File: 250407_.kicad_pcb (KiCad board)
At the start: 2 copper layers, 390 x 180.2 mm, 227 parts, among them CN1 KEYBOARD_20PIN_MALE, CN10 LED_CONNECTOR, CN2 USER_PORT_CON, CN3 CASSETTE_PORT_CON, CN4 SERIAL_BUS_CON, CN5 AV_CONN, CN6 EXPANSION_PORT, CN7 POWER_CON, CN8 CONTROL_PORT, CN9 CONTROL_PORT, M1 MODULATOR_LONGBOARD, Q1 2SC1815, Q2 2SC1815, Q3 TP298/2SD880, Q7 2SC1815, Q8 2SC1815, SW1 POWER_SWITCH, U1 CIA_U1, U10 4164-2, U11 4164-2, U12 4164-2, U13 74LS257, U14 74LS258, U15 74LS139, U16 4066_U28, U17 PLA_U17, U18 6581, U19 VIC, U2 CIA_U2, U20 556, U21 4164-2, U22 4164-2, U23 4164-2, U24 4164-2, U25 74LS257, U26 74LS373, U27 7408_U27, U28 4066_U28, U29 74LS74, U3 2364A, U30 74LS193, U31 74LS629N, U32 MC4044, U4 2364A, U5 2332A, U6 2114, U7 6510_MPU, U8 7406N, U9 4164-2, Y1 Crystal

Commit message: TP29B #2
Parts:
- Q3: value TP298/2SD880 -> TP29B/2SD880
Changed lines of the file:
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@@
       (effects (font (size 1.5 1.5) (thickness 0.25)))
     )
-    (fp_text value TP298/2SD880 (at 2.54 2) (layer F.Fab)
+    (fp_text value TP29B/2SD880 (at 2.54 2) (layer F.Fab)
       (effects (font (size 1 1) (thickness 0.15)))
     )

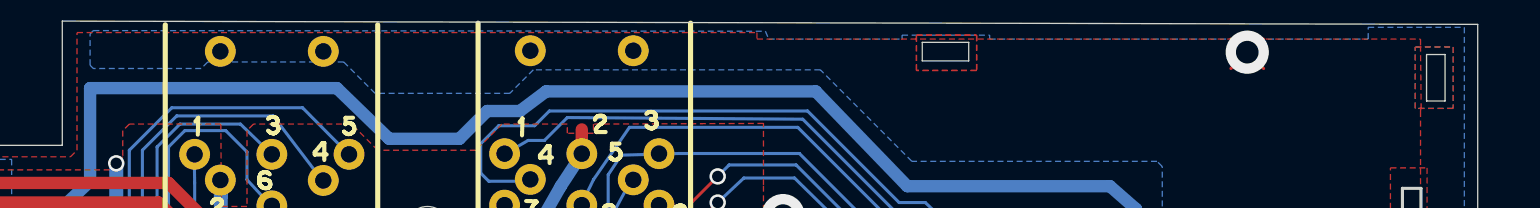
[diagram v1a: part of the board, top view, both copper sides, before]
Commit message: Fix north PCB edge
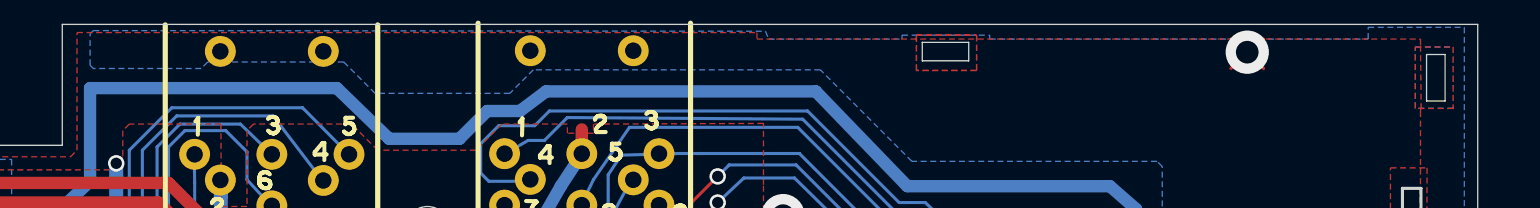
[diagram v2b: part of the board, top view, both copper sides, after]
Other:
- board size 390 x 180.2 mm -> 390 x 179.8 mm
